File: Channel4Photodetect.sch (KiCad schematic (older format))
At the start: 7 parts, among them U201 MCP6404, U202 LM339

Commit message: revised feedback resistor and updated reference voltage divider
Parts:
- removed R502: 22M, Resistors_SMD:R_0805_HandSoldering, symbol R_Small
- C501: value 2.2p -> 50p
- R501: value 22M -> 2M; Fieldname (none) -> Value; MPN RMCF0805FT22M0 -> (none)
- renumbered R503 to R502
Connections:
- net at C501.1, R502.2, U201.14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: now also R501.1
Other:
- moved on the sheet: R501
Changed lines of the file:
@@
 P 5420 2600
 F 0 "C501" V 5540 2560 50  0000 L CNN
-F 1 "2.2p" V 5310 2470 50  0000 L CNN
+F 1 "50p" V 5310 2470 50  0000 L CNN
 F 2 "Capacitors_SMD:C_0805_HandSoldering" H 5420 2600 50  0001 C CNN
 F 3 "" H 5420 2600 50  0000 C CNN
@@
 	5010 3750 5010 4050
 $Comp
-L R_Small R503
+L R_Small R502
 U 1 1 582296B8
 P 5820 4050
-F 0 "R503" V 5900 4010 50  0000 L CNN
+F 0 "R502" V 5900 4010 50  0000 L CNN
 F 1 "10K" V 5750 3930 50  0000 L CNN
 F 2 "Resistors_SMD:R_0805_HandSoldering" H 5820 4050 50  0001 C CNN
@@
 L R_Small R501
 U 1 1 5823CA83
-P 5190 3080
-F 0 "R501" V 5270 3040 50  0000 L CNN
-F 1 "22M" V 5120 2960 50  0000 L CNN
-F 2 "Resistors_SMD:R_0805_HandSoldering" H 5190 3080 50  0001 C CNN
-F 3 "" H 5190 3080 50  0000 C CNN
-F 4 "RMCF0805FT22M0" H 5190 3080 60  0001 C CNN "MPN"
-	1    5190 3080
-	0    1    1    0
-$EndComp
-$Comp
-L R_Small R502
-U 1 1 5823CA8B
-P 5520 3080
-F 0 "R502" V 5600 3040 50  0000 L CNN
-F 1 "22M" V 5450 2960 50  0000 L CNN
-F 2 "Resistors_SMD:R_0805_HandSoldering" H 5520 3080 50  0001 C CNN
-F 3 "" H 5520 3080 50  0000 C CNN
-F 4 "RMCF0805FT22M0" H 5520 3080 60  0001 C CNN "MPN"
-	1    5520 3080
+P 5440 3080
+F 0 "R501" V 5520 3040 50  0000 L CNN
+F 1 "2M" V 5370 2960 50  0000 L CNN
+F 2 "Resistors_SMD:R_0805_HandSoldering" H 5440 3080 50  0001 C CNN
+F 3 "" H 5440 3080 50  0000 C CNN
+F 4 "Value" H 5440 3080 60  0001 C CNN "Fieldname"
+	1    5440 3080
 	0    1    1    0
 $EndComp
 Wire Wire Line
-	5620 3080 5820 3080
+	5820 3080 5540 3080
 Wire Wire Line
-	5420 3080 5290 3080
-Wire Wire Line
-	5090 3080 5010 3080
+	5340 3080 5010 3080
 Connection ~ 5820 3080
 Connection ~ 5010 3080

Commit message: added pull-up resistors
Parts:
- added R503: 10K, Resistors_SMD:R_0805_HandSoldering, symbol R_Small
- R501: Fieldname Value -> (none); MPN (none) -> RC0805FR-072ML
- U202: MPN (none) -> LM339DE4
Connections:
- net PD4: now also R503.1
- new net +3V: R503.2
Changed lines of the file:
@@
 F 2 "Housings_SOIC:SOIC-14_3.9x8.7mm_Pitch1.27mm" H 6620 3850 50  0001 C CNN
 F 3 "" H 6720 3950 50  0000 C CNN
+F 4 "LM339DE4" H 6670 3750 60  0001 C CNN "MPN"
 	4    6670 3750
 	1    0    0    -1
@@
 F 2 "Resistors_SMD:R_0805_HandSoldering" H 5440 3080 50  0001 C CNN
 F 3 "" H 5440 3080 50  0000 C CNN
-F 4 "Value" H 5440 3080 60  0001 C CNN "Fieldname"
+F 4 "RC0805FR-072ML" H 5440 3080 60  0001 C CNN "MPN"
 	1    5440 3080
 	0    1    1    0
@@
 Connection ~ 5820 3080
 Connection ~ 5010 3080
+$Comp
+L R_Small R503
+U 1 1 5824D611
+P 7120 3500
+F 0 "R503" V 7200 3460 50  0000 L CNN
+F 1 "10K" V 7050 3380 50  0000 L CNN
+F 2 "Resistors_SMD:R_0805_HandSoldering" H 7120 3500 50  0001 C CNN
+F 3 "" H 7120 3500 50  0000 C CNN
+F 4 "RC0805FR-072ML" H 7120 3500 60  0001 C CNN "MPN"
+	1    7120 3500
+	-1   0    0    1
+$EndComp
+Text GLabel 7120 3250 1    60   Input ~ 0
++3V
+Wire Wire Line
+	7120 3250 7120 3400
+Wire Wire Line
+	7120 3600 7120 3750
+Connection ~ 7120 3750
 $EndSCHEMATC

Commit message: removed 10K resistors used as load for op amps
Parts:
- removed R502: 10K, Resistors_SMD:R_0805_HandSoldering, symbol R_Small
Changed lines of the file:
@@
 	5320 2600 5010 2600
-Wire Wire Line
-	5820 2600 5820 3950
 Wire Wire Line
 	5610 3650 6370 3650
@@
 	5520 2600 5820 2600
 $Comp
-L GND #PWR018
+L GND #PWR015
 U 1 1 582296B0
 P 5010 4050
-F 0 "#PWR018" H 5010 3800 50  0001 C CNN
+F 0 "#PWR015" H 5010 3800 50  0001 C CNN
 F 1 "GND" H 5010 3900 50  0000 C CNN
 F 2 "" H 5010 4050 50  0000 C CNN
@@
 Wire Wire Line
 	5010 3750 5010 4050
-$Comp
-L R_Small R502
-U 1 1 582296B8
-P 5820 4050
-F 0 "R502" V 5900 4010 50  0000 L CNN
-F 1 "10K" V 5750 3930 50  0000 L CNN
-F 2 "Resistors_SMD:R_0805_HandSoldering" H 5820 4050 50  0001 C CNN
-F 3 "" H 5820 4050 50  0000 C CNN
-F 4 "Value" H 5820 4050 60  0001 C CNN "Fieldname"
-	1    5820 4050
-	-1   0    0    1
-$EndComp
-Connection ~ 5820 3650
-$Comp
-L GND #PWR019
-U 1 1 582296C0
-P 5820 4250
-F 0 "#PWR019" H 5820 4000 50  0001 C CNN
-F 1 "GND" H 5820 4100 50  0000 C CNN
-F 2 "" H 5820 4250 50  0000 C CNN
-F 3 "" H 5820 4250 50  0000 C CNN
-	1    5820 4250
-	1    0    0    -1
-$EndComp
-Wire Wire Line
-	5820 4150 5820 4250
 $Comp
 L LM339 U202
@@
 	4400 3550 5010 3550
 $Comp
-L GND #PWR020
+L GND #PWR016
 U 1 1 58229702
 P 4450 4010
-F 0 "#PWR020" H 4450 3760 50  0001 C CNN
+F 0 "#PWR016" H 4450 3760 50  0001 C CNN
 F 1 "GND" H 4450 3860 50  0000 C CNN
 F 2 "" H 4450 4010 50  0000 C CNN
@@
 Wire Wire Line
 	5340 3080 5010 3080
-Connection ~ 5820 3080
 Connection ~ 5010 3080
 $Comp
@@
 	7120 3600 7120 3750
 Connection ~ 7120 3750
+Wire Wire Line
+	5820 2600 5820 3650
+Connection ~ 5820 3650
+Connection ~ 5820 3080
 $EndSCHEMATC

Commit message: replaced potentiometer with trimpot
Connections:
- net GND: now also U201.9 (-); no longer U201.13 (-)
- net at C501.1, R501.1, U202.9 (+): now also U201.8; no longer U201.14
- net at C501.2, PD501.1 (K), R501.2: now also U201.10 (+); no longer U201.12 (+)
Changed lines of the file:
@@
 $Comp
 L MCP6404 U201
-U 4 1 5822969F
+U 3 1 5822969F
 P 5310 3650
 F 0 "U201" H 5360 3850 50  0000 C CNN
@@
 F 2 "Housings_SOIC:SOIC-14_3.9x8.7mm_Pitch1.27mm" H 5260 3750 50  0001 C CNN
 F 3 "" H 5360 3850 50  0000 C CNN
-	4    5310 3650
+	3    5310 3650
 	1    0    0    -1
 $EndComp

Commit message: completed pcb basic layout
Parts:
- renumbered R503 to R502
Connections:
- net GND: now also U201.6 (-); no longer U201.9 (-)
- net at C501.1, R501.1, U202.9 (+): now also U201.7; no longer U201.8
- net at C501.2, PD501.1 (K), R501.2: now also U201.5 (+); no longer U201.10 (+)
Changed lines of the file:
@@
 $Comp
 L MCP6404 U201
-U 3 1 5822969F
+U 2 1 5822969F
 P 5310 3650
 F 0 "U201" H 5360 3850 50  0000 C CNN
@@
 F 2 "Housings_SOIC:SOIC-14_3.9x8.7mm_Pitch1.27mm" H 5260 3750 50  0001 C CNN
 F 3 "" H 5360 3850 50  0000 C CNN
-	3    5310 3650
+	2    5310 3650
 	1    0    0    -1
 $EndComp
@@
 	5520 2600 5820 2600
 $Comp
-L GND #PWR015
+L GND #PWR502
 U 1 1 582296B0
 P 5010 4050
-F 0 "#PWR015" H 5010 3800 50  0001 C CNN
+F 0 "#PWR502" H 5010 3800 50  0001 C CNN
 F 1 "GND" H 5010 3900 50  0000 C CNN
 F 2 "" H 5010 4050 50  0000 C CNN
@@
 	4400 3550 5010 3550
 $Comp
-L GND #PWR016
+L GND #PWR501
 U 1 1 58229702
 P 4450 4010
-F 0 "#PWR016" H 4450 3760 50  0001 C CNN
+F 0 "#PWR501" H 4450 3760 50  0001 C CNN
 F 1 "GND" H 4450 3860 50  0000 C CNN
 F 2 "" H 4450 4010 50  0000 C CNN
@@
 Connection ~ 5010 3080
 $Comp
-L R_Small R503
+L R_Small R502
 U 1 1 5824D611
 P 7120 3500
-F 0 "R503" V 7200 3460 50  0000 L CNN
+F 0 "R502" V 7200 3460 50  0000 L CNN
 F 1 "10K" V 7050 3380 50  0000 L CNN
 F 2 "Resistors_SMD:R_0805_HandSoldering" H 7120 3500 50  0001 C CNN

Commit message: changed photodiodes to BPW 34 S due to availability. Changed feedbak resistor and cap due to increased current output of diode.
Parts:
- C501: value 50p -> 100p
- PD501: value VBPW34S -> BPW 34 S-Z; AltPart (none) -> VBPW34S
- R501: value 2M -> 1M; Fieldname (none) -> Value; MPN RC0805FR-072ML -> (none)
- R502: Fieldname (none) -> Value; MPN RC0805FR-072ML -> (none)
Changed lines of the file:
@@
 P 5420 2600
 F 0 "C501" V 5540 2560 50  0000 L CNN
-F 1 "50p" V 5310 2470 50  0000 L CNN
+F 1 "100p" V 5310 2470 50  0000 L CNN
 F 2 "Capacitors_SMD:C_0805_HandSoldering" H 5420 2600 50  0001 C CNN
 F 3 "" H 5420 2600 50  0000 C CNN
@@
 	5520 2600 5820 2600
 $Comp
-L GND #PWR502
+L GND #PWR015
 U 1 1 582296B0
 P 5010 4050
-F 0 "#PWR502" H 5010 3800 50  0001 C CNN
+F 0 "#PWR015" H 5010 3800 50  0001 C CNN
 F 1 "GND" H 5010 3900 50  0000 C CNN
 F 2 "" H 5010 4050 50  0000 C CNN
@@
 P 4400 3760
 F 0 "PD501" H 4320 3840 50  0000 L CNN
-F 1 "VBPW34S" H 4250 3680 50  0000 L CNN
+F 1 "BPW 34 S-Z" H 4250 3680 50  0000 L CNN
 F 2 "DasBlinkinput:VBPW34S" V 4400 3760 50  0001 C CNN
-F 3 "http://www.vishay.com/docs/81128/vbpw34s.pdf" V 4400 3760 50  0001 C CNN
+F 3 "http://media.digikey.com/pdf/Data%20Sheets/Osram%20PDFs/bpw34_spdf.pdf" V 4400 3760 50  0001 C CNN
 F 4 "Value" H 4400 3760 60  0001 C CNN "Fieldname"
+F 5 "VBPW34S" H 4400 3760 60  0001 C CNN "AltPart"
 	1    4400 3760
 	0    1    1    0
@@
 	4400 3550 5010 3550
 $Comp
-L GND #PWR501
+L GND #PWR016
 U 1 1 58229702
 P 4450 4010
-F 0 "#PWR501" H 4450 3760 50  0001 C CNN
+F 0 "#PWR016" H 4450 3760 50  0001 C CNN
 F 1 "GND" H 4450 3860 50  0000 C CNN
 F 2 "" H 4450 4010 50  0000 C CNN
@@
 P 5440 3080
 F 0 "R501" V 5520 3040 50  0000 L CNN
-F 1 "2M" V 5370 2960 50  0000 L CNN
+F 1 "1M" V 5370 2960 50  0000 L CNN
 F 2 "Resistors_SMD:R_0805_HandSoldering" H 5440 3080 50  0001 C CNN
 F 3 "" H 5440 3080 50  0000 C CNN
-F 4 "RC0805FR-072ML" H 5440 3080 60  0001 C CNN "MPN"
+F 4 "Value" H 5440 3080 60  0001 C CNN "Fieldname"
+F 5 "   " H 5440 3080 60  0001 C CNN "MPN"
 	1    5440 3080
 	0    1    1    0
@@
 F 2 "Resistors_SMD:R_0805_HandSoldering" H 7120 3500 50  0001 C CNN
 F 3 "" H 7120 3500 50  0000 C CNN
-F 4 "RC0805FR-072ML" H 7120 3500 60  0001 C CNN "MPN"
+F 4 "Value" H 7120 3500 60  0001 C CNN "Fieldname"
 	1    7120 3500
 	-1   0    0    1

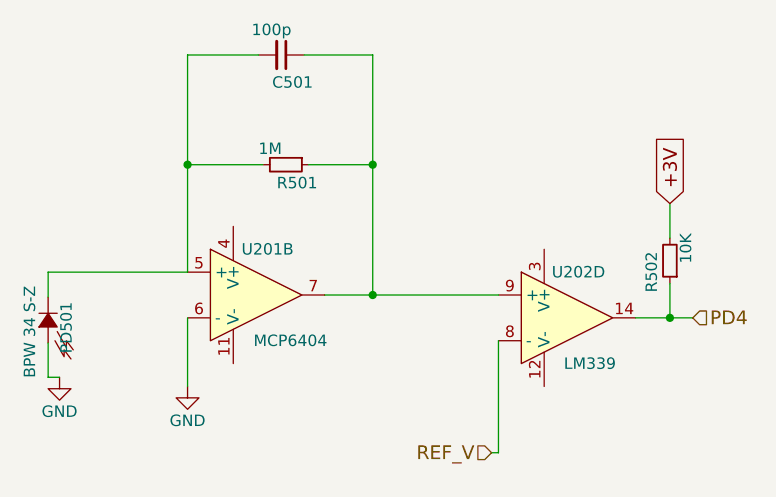
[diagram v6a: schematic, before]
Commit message: added test points at outputs of op-amps
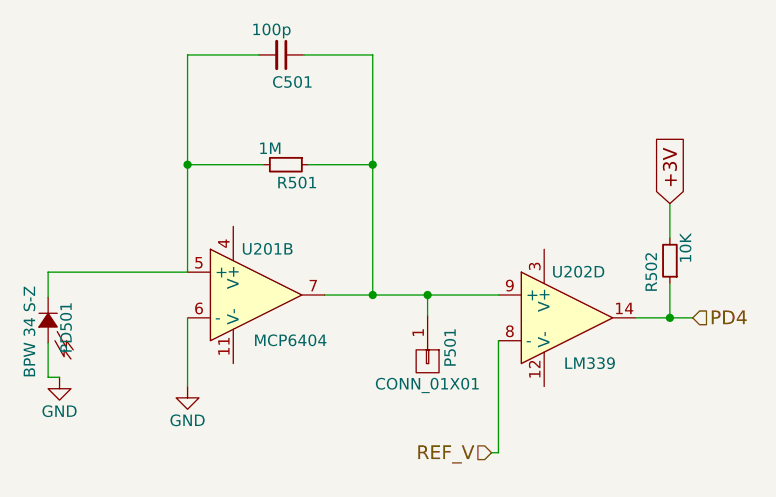
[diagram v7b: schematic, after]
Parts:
- added P501: CONN_01X01, Pin_Headers:Pin_Header_Straight_1x01, symbol CONN_01X01
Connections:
- net at C501.1, R501.1, U201.7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: now also P501.1 (P1)
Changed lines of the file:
@@
 Connection ~ 5820 3650
 Connection ~ 5820 3080
+$Comp
+L CONN_01X01 P501
+U 1 1 585447CD
+P 6060 3940
+F 0 "P501" H 6000 4040 50  0000 C CNN
+F 1 "CONN_01X01" V 6160 3940 50  0000 C CNN
+F 2 "Pin_Headers:Pin_Header_Straight_1x01" H 6060 3940 50  0001 C CNN
+F 3 "" H 6060 3940 50  0000 C CNN
+	1    6060 3940
+	0    1    1    0
+$EndComp
+Wire Wire Line
+	6060 3740 6060 3650
+Connection ~ 6060 3650
 $EndSCHEMATC

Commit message: corrected inputs on opamp and rerouted traces
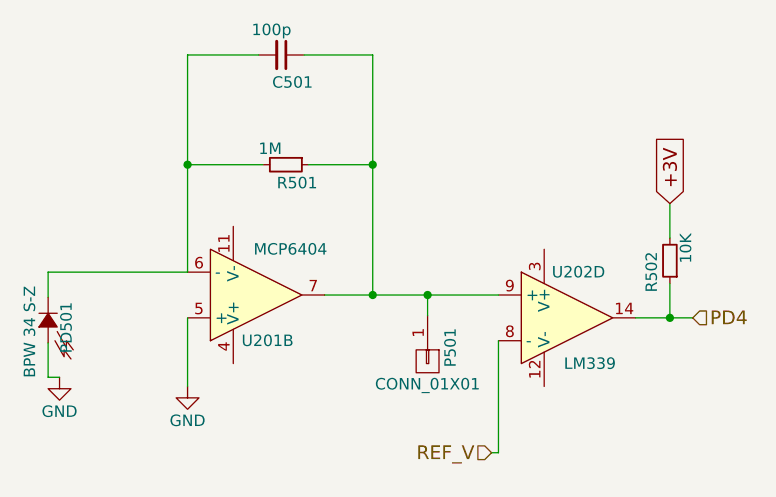
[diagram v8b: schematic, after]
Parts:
- U201, U202: footprint Housings_SOIC:SOIC-14_3.9x8.7mm_Pitch1.27mm -> DasBlinkinput:SOIC-14_3.9x8.7mm_Pitch1.27mm
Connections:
- net GND: now also U201.5 (+); no longer U201.6 (-)
- net at C501.2, PD501.1 (K), R501.2: now also U201.6 (-); no longer U201.5 (+)
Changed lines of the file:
@@
 F 0 "U201" H 5360 3850 50  0000 C CNN
 F 1 "MCP6404" H 5460 3450 50  0000 C CNN
-F 2 "Housings_SOIC:SOIC-14_3.9x8.7mm_Pitch1.27mm" H 5260 3750 50  0001 C CNN
+F 2 "DasBlinkinput:SOIC-14_3.9x8.7mm_Pitch1.27mm" H 5260 3750 50  0001 C CNN
 F 3 "" H 5360 3850 50  0000 C CNN
 	2    5310 3650
-	1    0    0    -1
+	1    0    0    1
 $EndComp
 Wire Wire Line
@@
 F 0 "U202" H 6720 3950 50  0000 C CNN
 F 1 "LM339" H 6770 3550 50  0000 C CNN
-F 2 "Housings_SOIC:SOIC-14_3.9x8.7mm_Pitch1.27mm" H 6620 3850 50  0001 C CNN
+F 2 "DasBlinkinput:SOIC-14_3.9x8.7mm_Pitch1.27mm" H 6620 3850 50  0001 C CNN
 F 3 "" H 6720 3950 50  0000 C CNN
 F 4 "LM339DE4" H 6670 3750 60  0001 C CNN "MPN"
